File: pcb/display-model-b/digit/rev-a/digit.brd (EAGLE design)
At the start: 26.7 x 40.6 mm, 54 parts, among them J1 DL-100-HEADER-02-EDGE, J10 SOLDER_JUMPER_3, J11 SOLDER_JUMPER_3, J2 DL-100-HEADER-02-EDGE, Q1 MMBT3904, Q2 MMBT3904, Q3 MMBT3904, Q4 MMBT3904, Q5 MMBT3904, Q6 MMBT3904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

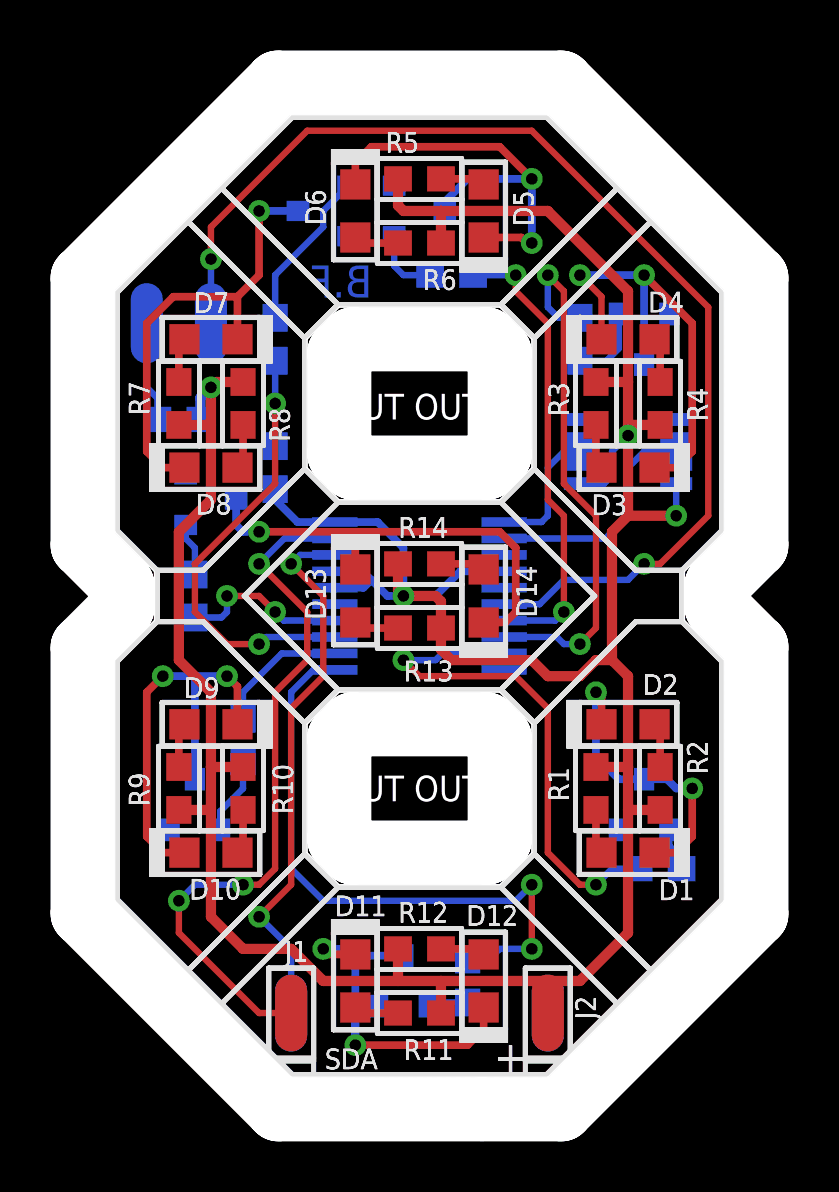
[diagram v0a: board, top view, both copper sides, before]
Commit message: Corrected drawings of touch panel PCB
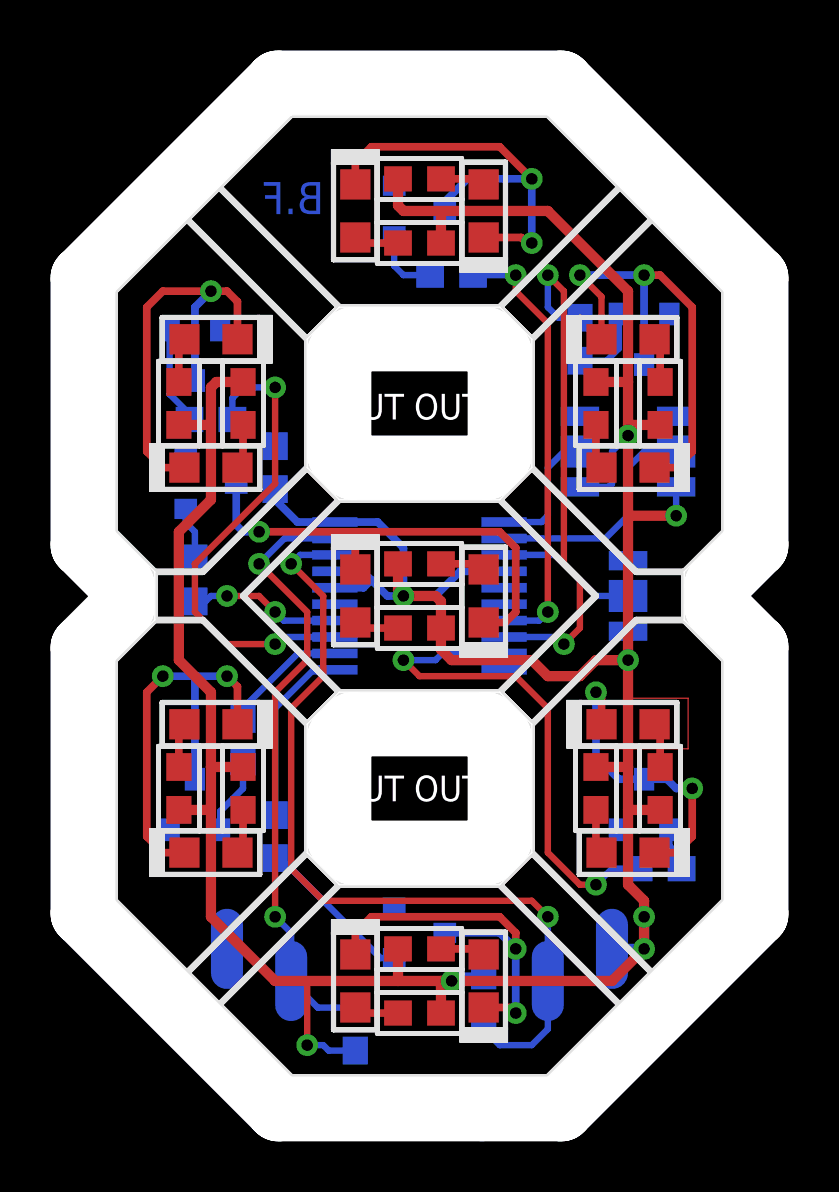
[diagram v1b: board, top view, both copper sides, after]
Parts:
- removed J10, J11: SOLDER_JUMPER_3, Misc:SOLDER_JUMPER_3
- removed U$3: (no value), Symbols:INFO_REV
- removed W5, W6: (no value), Misc:WIRE_SMT
- added J3: SOLDER_JUMPER_3, Misc:SOLDER_JUMPER_3
- added R16: N/A, Passive:SMD_0603
- added W1, W2, W3, W4: (no value), Misc:WIRE_SMT
- J1, J2: value DL-100-HEADER-02-EDGE -> SOLDER_JUMPER_3; device Connectors:HDR100-EDGE-2 -> Misc:SOLDER_JUMPER_3
- moved J1 26.9 mm to (22.2, 24.8), flipped to the bottom, turned to 90 degrees
- moved R15 25.1 mm to (9.53, 1.91), turned to 270 degrees
- moved J2 22.3 mm to (18.4, 24.8), flipped to the bottom, turned to 90 degrees
- moved R20 9.53 mm to (6.35, 9.53)
- moved Q4 7.65 mm to (3.17, 28.6), turned to 180 degrees
- moved R22 4.07 mm to (3.81, 26.0), turned to 0 degrees
- moved U$2 3.81 mm to (7.05, 34.8)
- moved U$1 2.62 mm to (18.2, 33.5)
- moved Q6 2.01 mm to (12.1, 5.71), turned to 90 degrees
- moved Q7 0.64 mm to (3.81, 23.5)
- moved R23 0.63 mm to (3.17, 19.7)
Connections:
- removed net EXT: U1.6, W5.1
- removed net N$30: R15.1, W6.1
- new net A2: J3.2, U1.3
- net 3.3V: now also J1.1, J2.1, J3.1, R16.2, W1.1; no longer J10.1, J11.1, J2.2
- net A0: now also J2.2; no longer J10.2
- net A1: now also J1.2; no longer J11.2
- net GND: now also J1.3, J2.3, J3.3, W4.1; no longer J10.3, J11.3, J2.1, U1.3
- net SCL: now also R16.1, W3.1; no longer J1.1
- net SDA: now also R15.1, W2.1; no longer J1.2
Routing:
- net EXT: track 45.8 -> 0.00 mm, vias 2 -> 0
- net SEG_D: track 24.6 -> 7.22 mm, vias 2 -> 0
- net SCL: track 21.8 -> 33.9 mm
- net 3.3V: track 130.6 -> 140.0 mm, vias 4 -> 8
- net N$29: track 0.00 -> 8.00 mm
- net A2: track 0.00 -> 5.58 mm
- net N$25: track 1.69 -> 6.81 mm
- net N$30: track 3.98 -> 0.00 mm
- net SDA: track 28.2 -> 24.5 mm, vias 3 -> 2
- net N$27: track 6.43 -> 3.87 mm
- net SEG_F: track 17.4 -> 19.1 mm
- net N$2: track 17.8 -> 16.8 mm
- net SEG_A: track 18.3 -> 17.4 mm
- net SEG_B: track 21.5 -> 20.6 mm
- net SEG_G: track 6.67 -> 6.03 mm
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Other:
- outline, holes or cut-outs redrawn
- board text added: "09/14"
- board text added: "A2"
- board text added: "R16"
- board text added: "Rev. A"
- board text removed: "10/14"
- board text removed: "B"
- board text removed: "BASE PCB"
- board text removed: "D1"
- board text removed: "D10"
- board text removed: "D11"
- board text removed: "D12"
- board text removed: "D13"
- board text removed: "D14"
- board text removed: "D2"
- board text removed: "D3"
- board text removed: "D4"
- board text removed: "D5"
- board text removed: "D6"
- board text removed: "D7"
- board text removed: "D8"
- board text removed: "D9"
- board text removed: "J1"
- board text removed: "J2"
- board text removed: "R1"
- board text removed: "R10"
- board text removed: "R11"
- board text removed: "R12"
- board text removed: "R13"
- board text removed: "R14"
- board text removed: "R2"
- board text removed: "R3"
- board text removed: "R4"
- board text removed: "R5"
- board text removed: "R6"
- board text removed: "R7"
- board text removed: "R8"
- board text removed: "R9"
- board text removed: "Rev."
